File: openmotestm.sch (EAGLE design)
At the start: 58 parts

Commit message: add sch and brd
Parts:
- removed U$10, U$11, U$12, U$13, U$14, U$15, U$16, U$17, U$18: TAP, openmotestm:TAP
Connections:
- removed net PB5: U$10.TAP, U$7.PB5
- net PA11: now also U$8.CTS; no longer U$14.TAP
- net PA12: now also U$8.RTS; no longer U$13.TAP
- net PA3: no longer U$18.TAP
- net PA8: no longer U$15.TAP
- net PB8: no longer R5.1
- net PB9: no longer R6.1
- net PC1: no longer U$8.RTS
- net PC10: now also R6.1
- net PC11: now also R5.1; no longer U$12.TAP
- net PC12: no longer U$11.TAP
- net PC2: no longer R7.1
- net PC3: no longer R8.1
- net PC6: now also R8.1; no longer U$17.TAP
- net PC7: now also R7.1; no longer U$16.TAP
- net PD2: no longer U$8.CTS

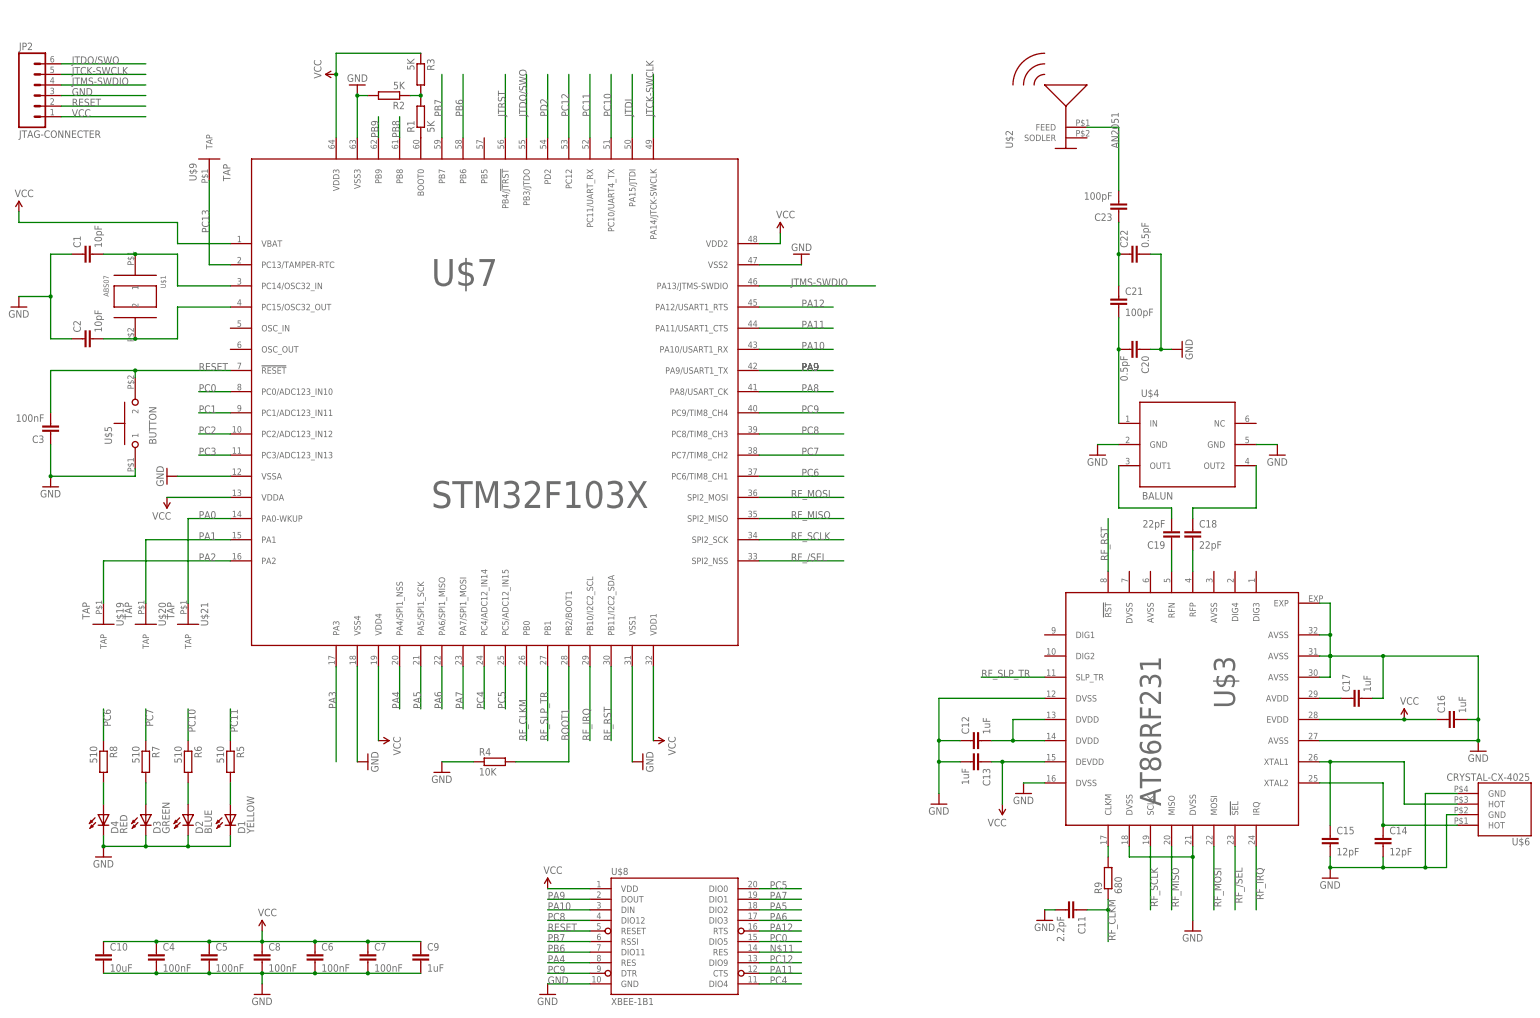
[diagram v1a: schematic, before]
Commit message: change the footprint of capacity larger than 1uF to 0603 footprint. Update 3D sketchUp model
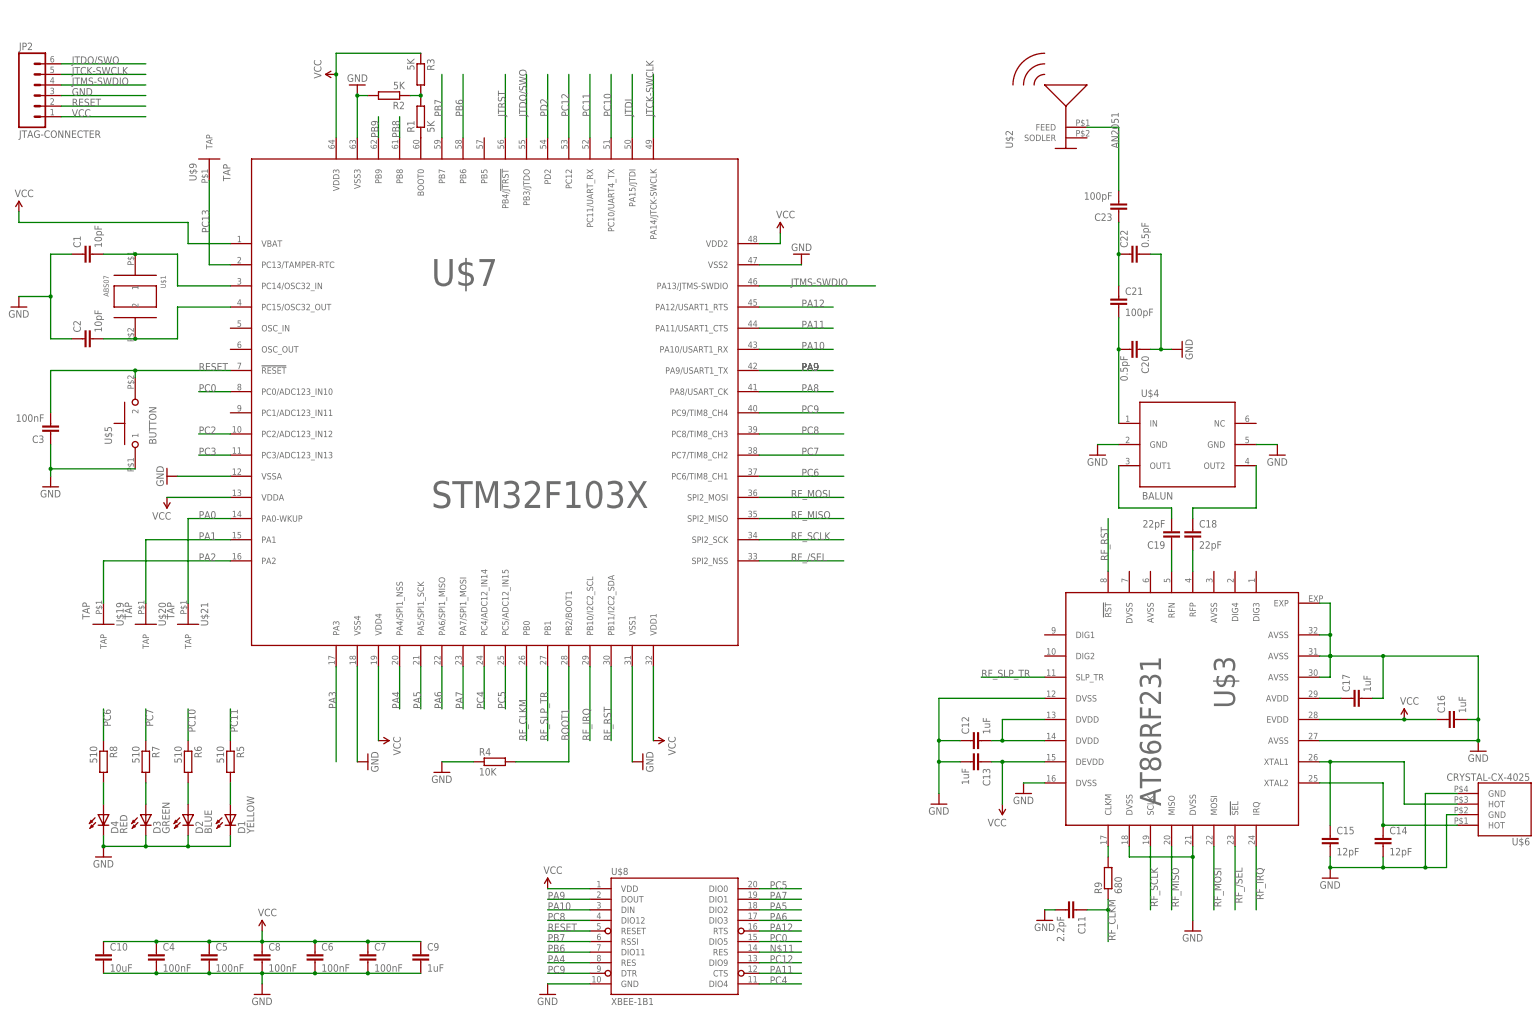
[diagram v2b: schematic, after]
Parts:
- C10, C12, C13, C16, C17, C9: device rcl:C-EUC0402 -> rcl:C-EUC0603
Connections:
- removed net PC1: U$7.PC1/ADC123_IN11

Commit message: change the pcb to satisfy minimum clearance of 5 mil
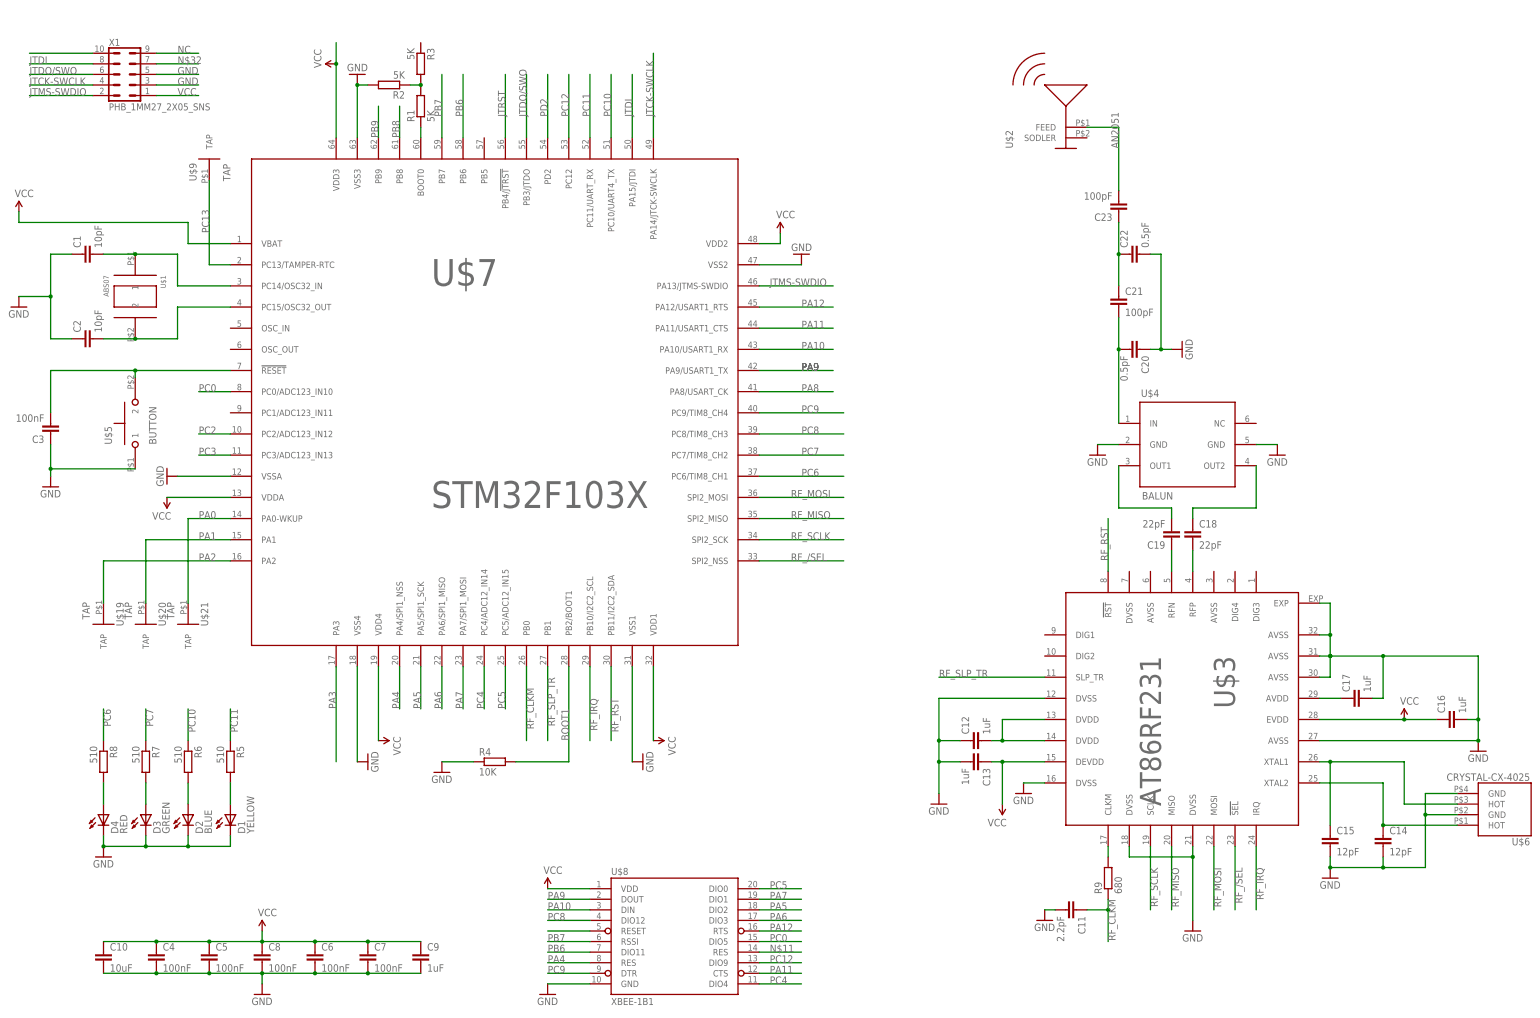
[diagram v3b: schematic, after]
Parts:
- removed JP2: JTAG-CONNECTER, SparkFun-Connectors:M06SMD_MALE
- added X1: PHB_1MM27_2X05_SNS, _hhn_con_pinhead_box_1mm27:PHB_1MM27_2X05_SNS
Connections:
- new net N$32: X1.7
- new net NC: X1.9
- net GND: now also X1.3, X1.5; no longer JP2.3
- net JTCK-SWCLK: now also X1.4; no longer JP2.5
- net JTDI: now also X1.8
- net JTDO/SWO: now also X1.6; no longer JP2.6
- net JTMS-SWDIO: now also X1.2; no longer JP2.4
- net RESET: now also X1.10; no longer JP2.2
- net VCC: now also X1.1; no longer JP2.1, R3.1
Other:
- moved on the sheet: R1, R2, R3

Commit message: update openmotestm
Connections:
- net VCC: now also R3.1
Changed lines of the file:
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@@
 <junction x="-93.98" y="124.46"/>
 <pinref part="U$7" gate="G$1" pin="VDD3"/>
+<pinref part="R3" gate="G$1" pin="1"/>
+<wire x1="-93.98" y1="129.54" x2="-73.66" y2="129.54" width="0.1524" layer="91"/>
 </segment>
 <segment>
@@
 <pinref part="X1" gate="G$1" pin="10"/>
 <wire x1="-167.64" y1="127" x2="-152.4" y2="127" width="0.1524" layer="91"/>
+<label x="-167.64" y="127" size="1.778" layer="95"/>
 </segment>
 <segment>
 <pinref part="U$8" gate="G$1" pin="RESET"/>
 <wire x1="-43.18" y1="-83.82" x2="-33.02" y2="-83.82" width="0.1524" layer="91"/>
+<label x="-43.18" y="-83.82" size="1.778" layer="95"/>
 </segment>
 <segment>
@@
 <wire x1="-162.56" y1="50.8" x2="-142.24" y2="50.8" width="0.1524" layer="91"/>
 <junction x="-142.24" y="50.8"/>
-</segment>
-</net>
+<label x="-134.62" y="50.8" size="1.778" layer="95"/>
+</segment>
+</net>

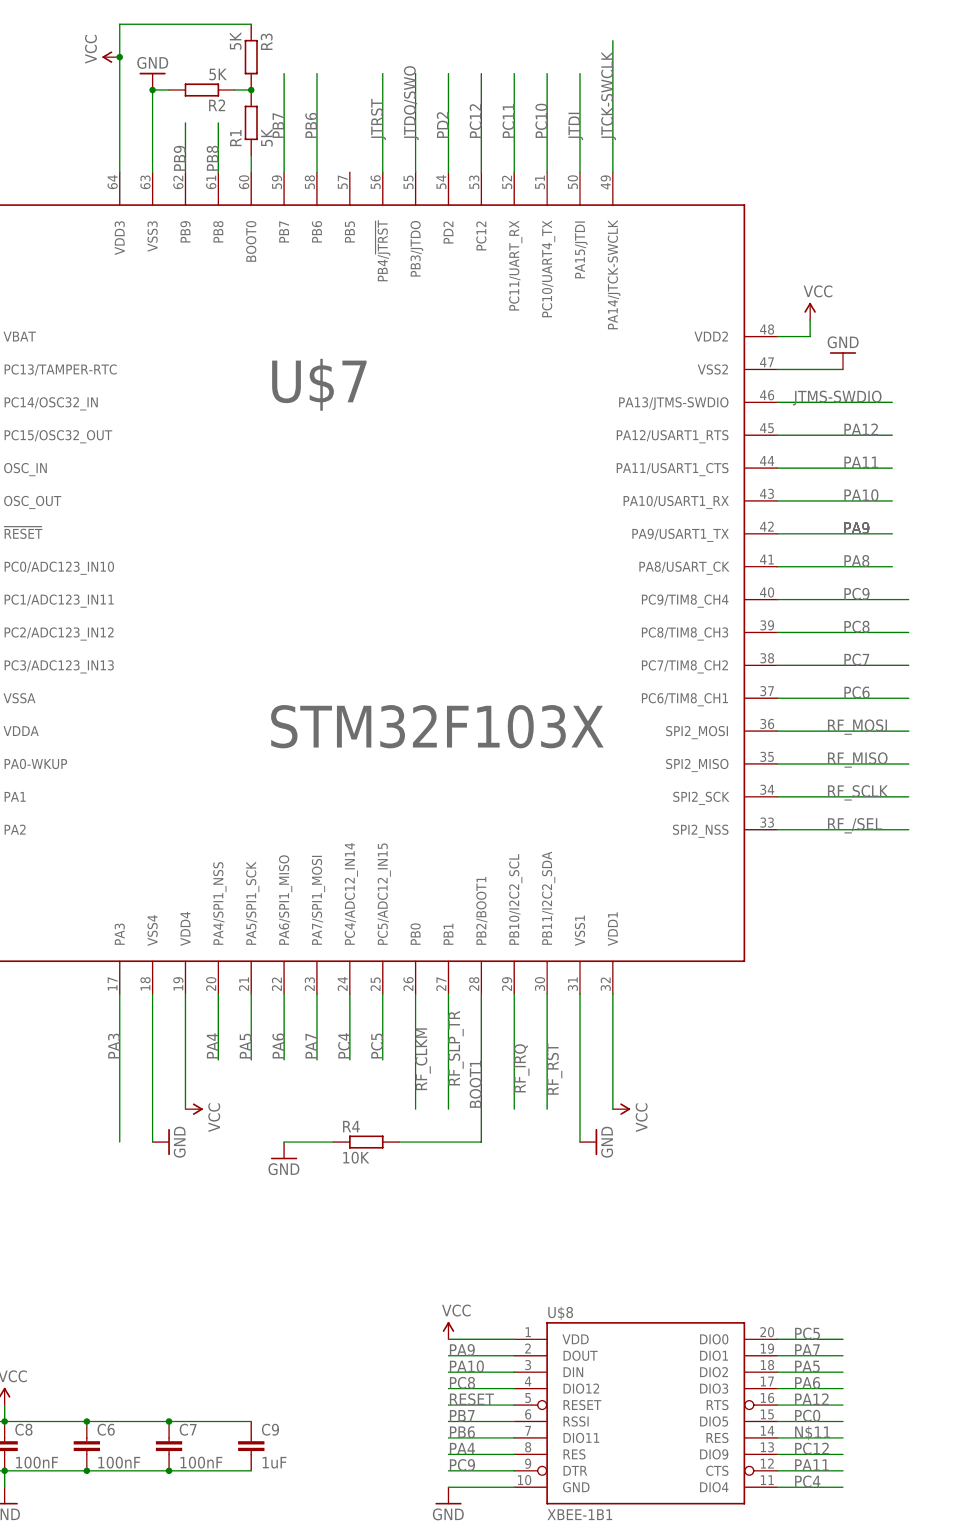
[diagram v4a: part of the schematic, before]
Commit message: Add XBee-Explorer-Dongle-Sparkfun. Update openmotestm. arrange the layout of openquadcopter board.
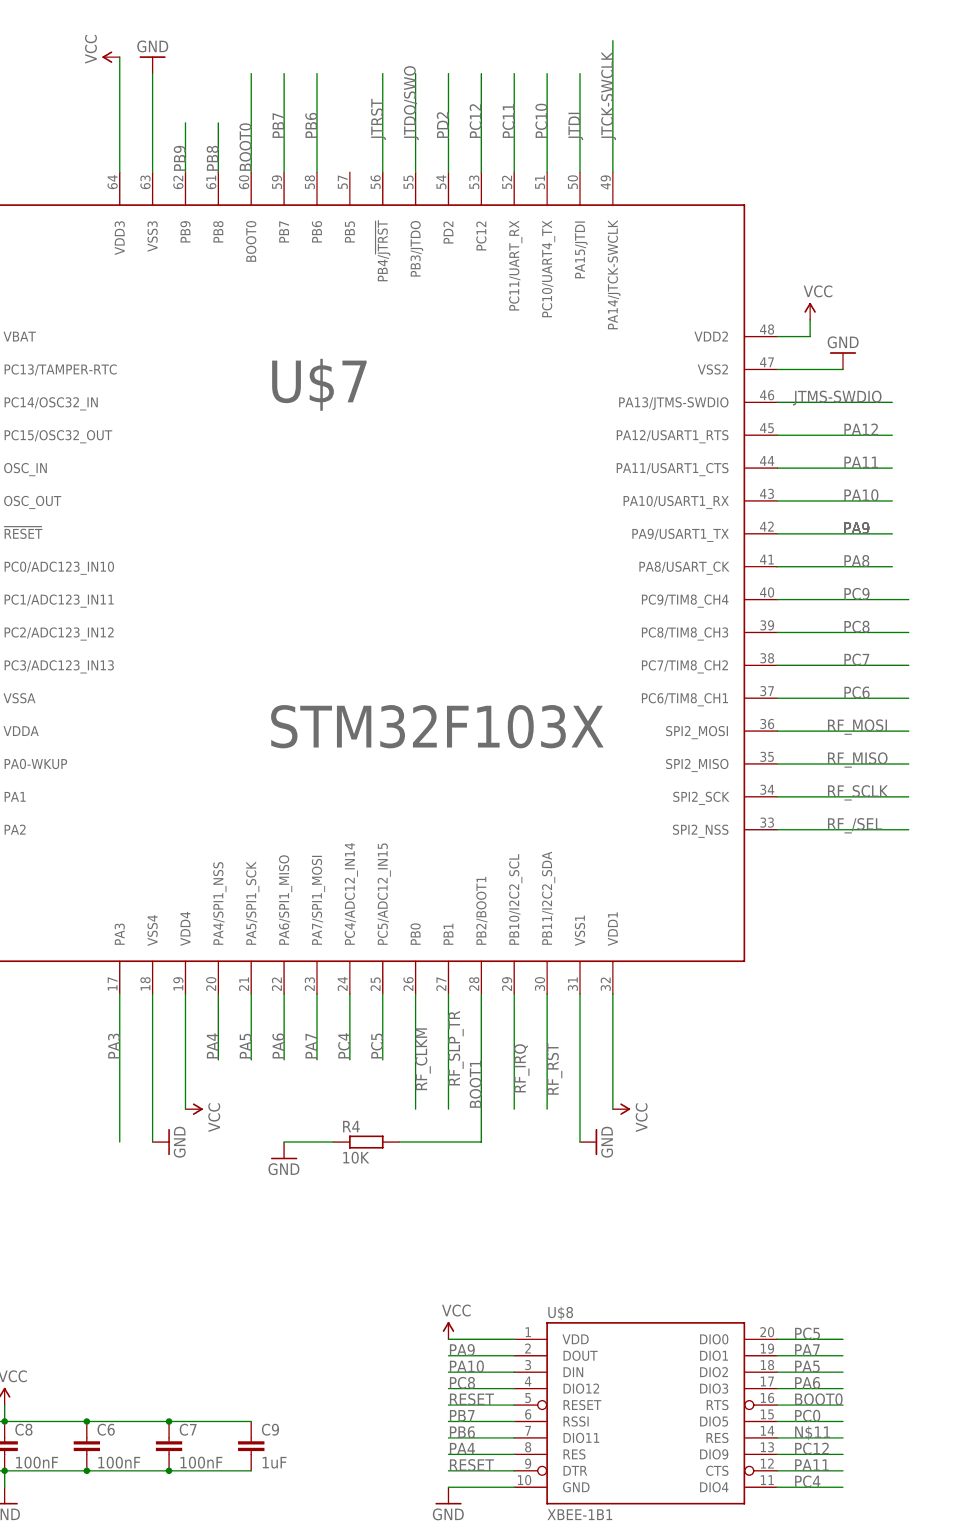
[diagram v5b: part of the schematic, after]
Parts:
- removed R1, R2, R3: 5K, rcl:R-EU_R0402
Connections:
- removed net N$3: R1.1, U$7.BOOT0
- removed net N$4: R1.2, R2.1, R3.2
- new net BOOT0: U$7.BOOT0, U$8.RTS
- net GND: no longer R2.2
- net PA12: no longer U$8.RTS
- net PC9: no longer U$8.DTR
- net RESET: now also U$8.DTR
- net VCC: no longer R3.1
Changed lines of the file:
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@@
 <part name="C1" library="resistor" deviceset="C-EU" device="C0402" value="10pF"/>
 <part name="C2" library="resistor" deviceset="C-EU" device="C0402" value="10pF"/>
-<part name="R1" library="rcl" deviceset="R-EU_" device="R0402" value="5K"/>
-<part name="R2" library="rcl" deviceset="R-EU_" device="R0402" value="5K"/>
-<part name="R3" library="rcl" deviceset="R-EU_" device="R0402" value="5K"/>
 <part name="SUPPLY2" library="SparkFun-Aesthetics" deviceset="VCC" device=""/>
 <part name="GND2" library="SparkFun-Aesthetics" deviceset="GND" device=""/>
@@
 <instance part="C1" gate="G$1" x="-154.94" y="78.74" rot="R90"/>
 <instance part="C2" gate="G$1" x="-154.94" y="58.42" rot="R90"/>
-<instance part="R1" gate="G$1" x="-73.66" y="114.3" rot="R90"/>
-<instance part="R2" gate="G$1" x="-81.28" y="119.38" rot="R180"/>
-<instance part="R3" gate="G$1" x="-73.66" y="124.46" rot="R270"/>
 <instance part="SUPPLY2" gate="G$1" x="-93.98" y="124.46" rot="R90"/>
-<instance part="GND2" gate="1" x="-88.9" y="121.92" rot="R180"/>
+<instance part="GND2" gate="1" x="-88.9" y="124.46" rot="R180"/>
 <instance part="C3" gate="G$1" x="-162.56" y="35.56" rot="R180"/>
 <instance part="GND3" gate="1" x="-162.56" y="22.86"/>
@@
 </segment>
 <segment>
-<pinref part="R2" gate="G$1" pin="2"/>
-<wire x1="-86.36" y1="119.38" x2="-88.9" y2="119.38" width="0.1524" layer="91"/>
 <pinref part="GND2" gate="1" pin="GND"/>
-<wire x1="-88.9" y1="106.68" x2="-88.9" y2="119.38" width="0.1524" layer="91"/>
-<junction x="-88.9" y="119.38"/>
+<wire x1="-88.9" y1="106.68" x2="-88.9" y2="121.92" width="0.1524" layer="91"/>
 <pinref part="U$7" gate="G$1" pin="VSS3"/>
 </segment>
@@
 <segment>
 <pinref part="SUPPLY2" gate="G$1" pin="VCC"/>
-<wire x1="-93.98" y1="129.54" x2="-93.98" y2="124.46" width="0.1524" layer="91"/>
 <wire x1="-93.98" y1="124.46" x2="-93.98" y2="106.68" width="0.1524" layer="91"/>
-<junction x="-93.98" y="124.46"/>
 <pinref part="U$7" gate="G$1" pin="VDD3"/>
-<pinref part="R3" gate="G$1" pin="1"/>
-<wire x1="-93.98" y1="129.54" x2="-73.66" y2="129.54" width="0.1524" layer="91"/>
 </segment>
 <segment>
@@
 </segment>
 </net>
-<net name="N$4" class="0">
-<segment>
-<pinref part="R2" gate="G$1" pin="1"/>
-<pinref part="R3" gate="G$1" pin="2"/>
-<pinref part="R1" gate="G$1" pin="2"/>
-<junction x="-73.66" y="119.38"/>
-<wire x1="-73.66" y1="119.38" x2="-76.2" y2="119.38" width="0.1524" layer="91"/>
-</segment>
-</net>
 <net name="BOOT1" class="0">
 <segment>
@@
 </net>
 <net name="PC9" class="0">
-<segment>
-<pinref part="U$8" gate="G$1" pin="DTR"/>
-<wire x1="-43.18" y1="-93.98" x2="-33.02" y2="-93.98" width="0.1524" layer="91"/>
-<label x="-43.18" y="-93.98" size="1.778" layer="95"/>
-</segment>
 <segment>
 <wire x1="7.62" y1="40.64" x2="27.94" y2="40.64" width="0.1524" layer="91"/>
@@
 </segment>
 </net>
-<net name="N$3" class="0">
-<segment>
-<pinref part="R1" gate="G$1" pin="1"/>
-<pinref part="U$7" gate="G$1" pin="BOOT0"/>
-<wire x1="-73.66" y1="109.22" x2="-73.66" y2="106.68" width="0.1524" layer="91"/>
-</segment>
-</net>
 <net name="PA12" class="0">
 <segment>
@@
 <wire x1="7.62" y1="66.04" x2="25.4" y2="66.04" width="0.1524" layer="91"/>
 <label x="17.78" y="66.04" size="1.778" layer="95"/>
-</segment>
-<segment>
-<pinref part="U$8" gate="G$1" pin="RTS"/>
-<wire x1="7.62" y1="-83.82" x2="17.78" y2="-83.82" width="0.1524" layer="91"/>
-<label x="10.16" y="-83.82" size="1.778" layer="95"/>
 </segment>
 </net>
@@
 <label x="-134.62" y="50.8" size="1.778" layer="95"/>
 </segment>
+<segment>
+<pinref part="U$8" gate="G$1" pin="DTR"/>
+<wire x1="-43.18" y1="-93.98" x2="-33.02" y2="-93.98" width="0.1524" layer="91"/>
+<label x="-43.18" y="-93.98" size="1.778" layer="95"/>
+</segment>
 </net>
 <net name="N$5" class="0">
@@
 </segment>
 </net>
+<net name="BOOT0" class="0">
+<segment>
+<pinref part="U$8" gate="G$1" pin="RTS"/>
+<wire x1="7.62" y1="-83.82" x2="17.78" y2="-83.82" width="0.1524" layer="91"/>
+<label x="10.16" y="-83.82" size="1.778" layer="95"/>
+</segment>
+<segment>
+<pinref part="U$7" gate="G$1" pin="BOOT0"/>
+<wire x1="-73.66" y1="106.68" x2="-73.66" y2="121.92" width="0.1524" layer="91"/>
+<label x="-73.66" y="106.68" size="1.778" layer="95" rot="R90"/>
+</segment>
+</net>
